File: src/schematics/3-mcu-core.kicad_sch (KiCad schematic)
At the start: 116 parts, among them Q301 NX6008NBKW, U301 PIC32CX1025SG41100-I/E5X, U302 AP22653AW6

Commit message: Added part numbers for the capacitors.
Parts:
- C301, C302, C303, C304, C305, C306, C307, C309, C310, C311, C312, C313, C314, C322, C326, C327, C328, C329, C330, C331, C332, C333, C334, C335, C336, C337, C338, C339, C340, C341, C342, C343, C344, C345, C346, C347, C348, C349, C350: ManufacturerPartNumber (none) -> CL05A475MP5NRNC
- C321: Manufacturer (none) -> Samsung; Manufacturer2 (none) -> Samsung; Manufacturer2PartNumber (none) -> CL05A104KA5NNNC; ManufacturerPartNumber (none) -> CL05B104KA5NNNC
- FB301: Package (none) -> WLBD2012

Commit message: Added part numbers for the resistors.
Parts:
- R301, R302, R303, R304: Manufacturer (none) -> Walsin; Manufacturer2 (none) -> Yageo; Manufacturer2PartNumber (none) -> RC0402FR-0710KL; ManufacturerPartNumber (none) -> WR04X1002FTL
- R305, R306, R320: Manufacturer (none) -> Walsin; Manufacturer2 (none) -> Yageo; Manufacturer2PartNumber (none) -> RC0402FR-071KL; ManufacturerPartNumber (none) -> WR04X1001FTL
- R307, R309: Manufacturer (none) -> Yageo; Manufacturer2 (none) -> Walsin; Manufacturer2PartNumber (none) -> WR04X000PTL; ManufacturerPartNumber (none) -> RC0402FR-070RL
- R310, R332, R333, R348, R349, R350: Manufacturer (none) -> Walsin; Manufacturer2 (none) -> Yageo; Manufacturer2PartNumber (none) -> RC0402FR-0733KL; ManufacturerPartNumber (none) -> WR04X3302FTL
- R311, R312, R313, R314, R315, R316, R317, R321, R322, R323, R324, R325, R326, R327, R328, R329, R330, R331, R336, R337, R338, R339, R340: Manufacturer (none) -> Yageo; Manufacturer2 (none) -> Bourns; Manufacturer2PartNumber (none) -> CR0402-FX-43R0GLF; ManufacturerPartNumber (none) -> RC0402FR-0743RL
- R318, R319, R346, R347: Manufacturer (none) -> Yageo; Manufacturer2 (none) -> Walsin; Manufacturer2PartNumber (none) -> MR04X1801FTL; ManufacturerPartNumber (none) -> RC0402FR-071K8L
- R334, R335: Manufacturer (none) -> Walsin; Manufacturer2 (none) -> Yageo; Manufacturer2PartNumber (none) -> RC0402FR-07330RL; ManufacturerPartNumber (none) -> WR04X3300FTL
- R341, R342, R343, R344, R345: Manufacturer (none) -> Yageo; Manufacturer2 (none) -> KOA Speer; Manufacturer2PartNumber (none) -> RK73H1ETTP41R2F; ManufacturerPartNumber (none) -> RC0402FR-0741R2L
- R351, R352: Manufacturer (none) -> Yageo; Manufacturer2 (none) -> Yageo; Manufacturer2PartNumber (none) -> AC0402DR-0739KL; ManufacturerPartNumber (none) -> RC0402FR-0739KL

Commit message: Started to clean up the ERC flags.
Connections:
- net at XTAL301.2: no longer XTAL301.4
- net at XTAL302.2: no longer XTAL302.4

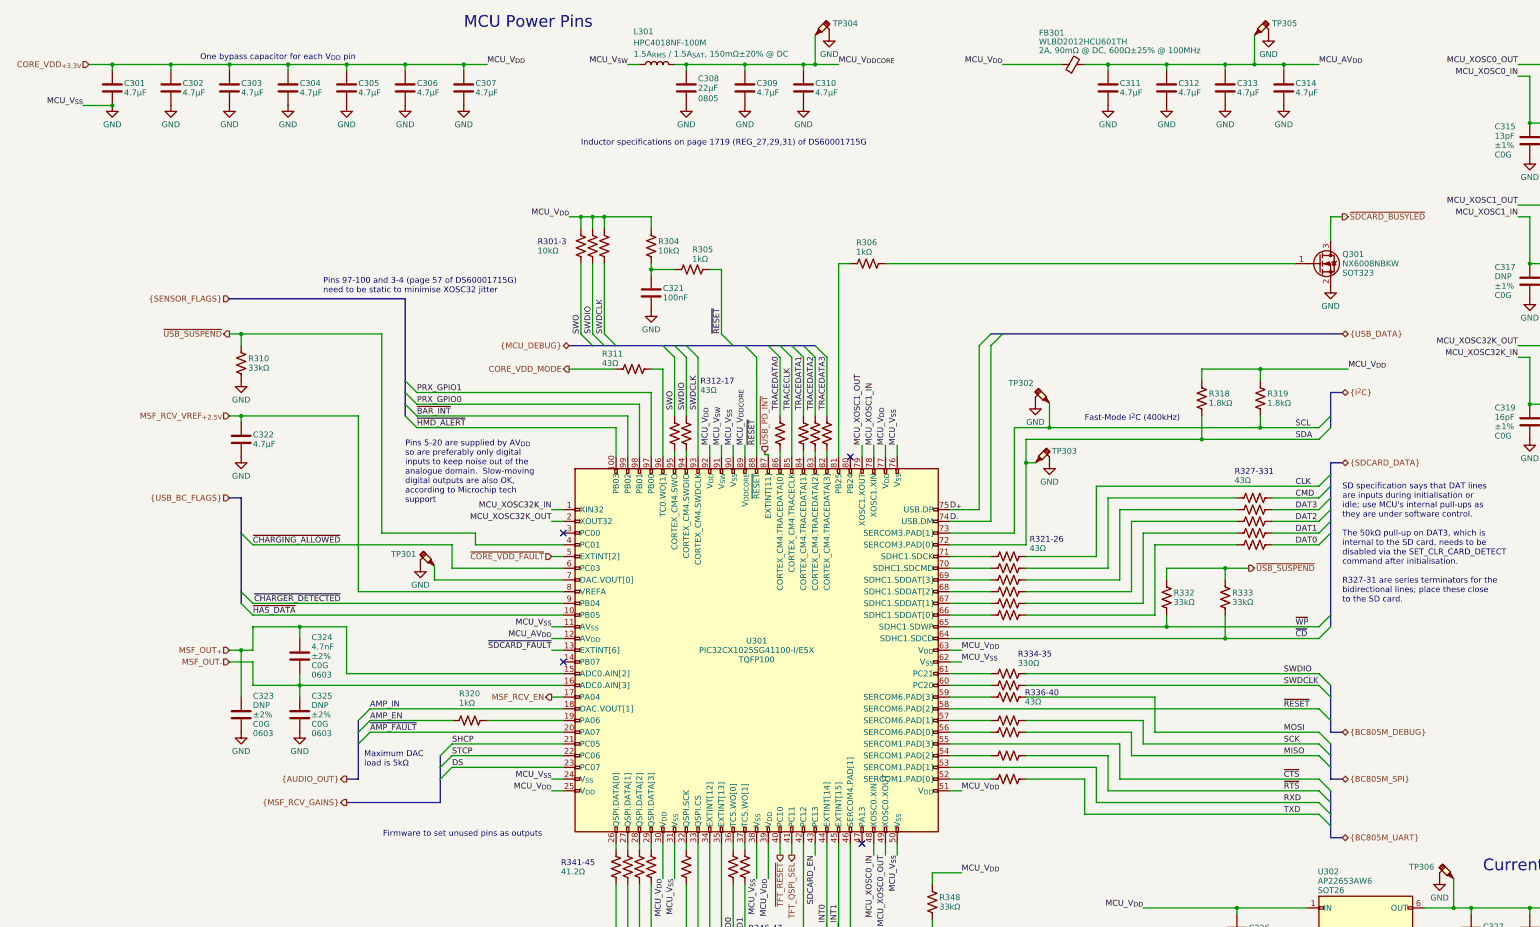
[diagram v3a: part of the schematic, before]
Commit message: Clean up the remaining ERC flags.
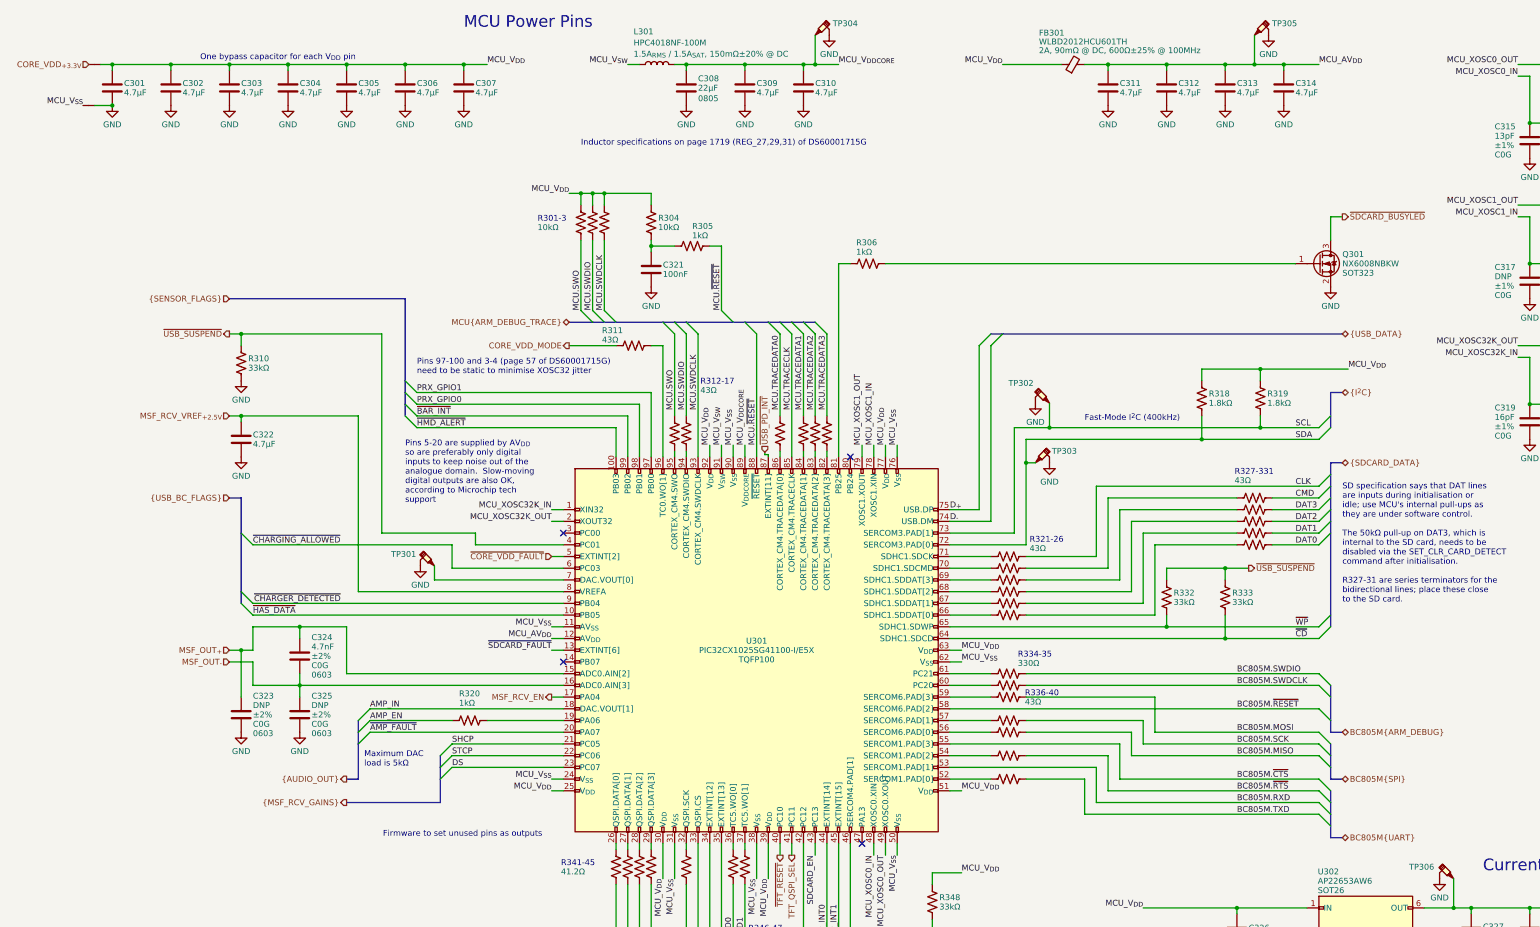
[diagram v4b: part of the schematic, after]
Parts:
- added NT301, NT302: Net Tie, restall-generic-wires:net-tie-2-6mil, symbol restall-generic-wires:net-tie-2
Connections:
- net CORE_VDD_{+3.3V}: now also NT301.1 (P1_PASSIVE); no longer C301.1, C302.1, C303.1, C304.1, C305.1, C306.1, C307.1, C326.1, C337.1, C338.1, C339.1, C340.1, C341.1, C342.1, C343.1, C344.1, C345.1, C346.1, C347.1, C348.1, C349.1, C350.1, FB301.1 (P1), R301.2, R302.2, R303.2, R304.1, R318.1, R319.1, R348.1, U301.25 (V_{DD}), U301.30 (V_{DD}), U301.39 (V_{DD}), U301.51 (V_{DD}), U301.63 (V_{DD}), U301.77 (V_{DD}), U301.92 (V_{DD}), U302.1 (IN)
- net SCK: no longer R337.2
- net GND renamed GND_PWRIN
- net GND_PWRIN: now also NT302.2 (P2_PASSIVE); no longer U301.101 (V_{SS}), U301.11 (AV_{SS}), U301.24 (V_{SS}), U301.31 (V_{SS}), U301.38 (V_{SS}), U301.50 (V_{SS}), U301.62 (V_{SS}), U301.76 (V_{SS}), U301.90 (V_{SS})
- net MISO renamed BC805M.MISO
- net MOSI renamed BC805M.MOSI
- net RXD renamed BC805M.RXD
- net SWDCLK renamed MCU.SWDCLK
- net MCU.SWDCLK: no longer R335.2
- net SWDIO renamed MCU.SWDIO
- net MCU.SWDIO: no longer R334.2
- net SWO renamed MCU.SWO
- net TRACECLK renamed MCU.TRACECLK
- net TRACEDATA0 renamed MCU.TRACEDATA0
- net TRACEDATA1 renamed MCU.TRACEDATA1
- net TRACEDATA2 renamed MCU.TRACEDATA2
- net TRACEDATA3 renamed MCU.TRACEDATA3
- net TXD renamed BC805M.TXD
- net ~{CTS} renamed BC805M.~{CTS}
- net ~{RESET} renamed MCU.~{RESET}
- net MCU.~{RESET}: no longer U301.58 (PC18)
- net ~{RTS} renamed BC805M.~{RTS}
- new net BC805M.SCK: R337.2
- new net BC805M.SWDCLK: R335.2
- new net BC805M.SWDIO: R334.2
- new net BC805M.~{RESET}: U301.58 (PC18)
- new net MCU_V_{DD}: C301.1, C302.1, C303.1, C304.1, C305.1, C306.1, C307.1, C326.1, C337.1, C338.1, C339.1, C340.1, C341.1, C342.1, C343.1, C344.1, C345.1, C346.1, C347.1, C348.1, C349.1, C350.1, FB301.1 (P1), NT301.2 (P2_PASSIVE), R301.2, R302.2, R303.2, R304.1, R318.1, R319.1, R348.1, U301.25 (V_{DD}), U301.30 (V_{DD}), U301.39 (V_{DD}), U301.51 (V_{DD}), U301.63 (V_{DD}), U301.77 (V_{DD}), U301.92 (V_{DD}), U302.1 (IN)
- new net MCU_V_{SS}: NT302.1 (P1_PASSIVE), U301.11 (AV_{SS}), U301.24 (V_{SS}), U301.31 (V_{SS}), U301.38 (V_{SS}), U301.50 (V_{SS}), U301.62 (V_{SS}), U301.76 (V_{SS}), U301.90 (V_{SS})
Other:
- moved on the sheet: C321, R304, R305, R311

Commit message: Started to lay out the PCB.
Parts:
- removed NT301, NT302: Net Tie, restall-generic-wires:net-tie-2-6mil, symbol restall-generic-wires:net-tie-2
- L301: value HPC4018NF-100M -> 10μH
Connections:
- net MCU_V_{DD} is gone; now on net CORE_VDD_{+3.3V}: C301.1, C302.1, C303.1, C304.1, C305.1, C306.1, C307.1, C326.1, C337.1, C338.1, C339.1, C340.1, C341.1, C342.1, C343.1, C344.1, C345.1, C346.1, C347.1, C348.1, C349.1, C350.1, FB301.1 (P1), R301.2, R302.2, R303.2, R304.1, R318.1, R319.1, R348.1, U301.25 (V_{DD}), U301.30 (V_{DD}), U301.39 (V_{DD}), U301.51 (V_{DD}), U301.63 (V_{DD}), U301.77 (V_{DD}), U301.92 (V_{DD}), U302.1 (IN)
- net MCU_V_{SS} is gone; now on net GND: U301.11 (AV_{SS}), U301.24 (V_{SS}), U301.31 (V_{SS}), U301.38 (V_{SS}), U301.50 (V_{SS}), U301.62 (V_{SS}), U301.76 (V_{SS}), U301.90 (V_{SS})
- net D_{+} renamed MCU.D+
- net D_{-} renamed MCU.D-
- net GND_PWRIN renamed GND
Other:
- note added: "TODO: GND_PWRIN IS ACTUALLY GND - HOW TO RENAME THE DAMN NET ?!?"

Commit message: Rearranged the SD Card and TVS placements.
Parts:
- removed R327, R328, R329, R330, R331: 43Ω, restall-generic-resistors:nominal-0402-1005, symbol restall-generic-resistors:resistor
- renumbered R332 to R327, R333 to R328, R334 to R329, R335 to R330, R336 to R331, R337 to R332, R338 to R333, R339 to R334, R340 to R335, R341 to R336, R342 to R337, R343 to R338, R344 to R339, R345 to R340, R346 to R341, R347 to R342, R348 to R343, R349 to R344, R350 to R345, R351 to R346, R352 to R347
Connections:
- net CMD: now also R322.2
- net DAT0: now also R326.2
- net DAT1: now also R325.2
- net DAT2: now also R324.2
- net DAT3: now also R323.2
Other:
- note added: "R329-30"
- note added: "R331-35"
- note added: "R341-42"
- note added: "SD specification says that DAT lines are inputs during initialisation or idle; use MCU's internal pull-ups as they are under software control. The 50kΩ pull-up on DAT3, which is internal to the SD card, needs to be disabled via the SET_CLR_CARD_DETECT command after initialisation."
- note removed: "R327-331"
- note removed: "R334-35"
- note removed: "R341-45"
- note removed: "R346-47"
- note removed: "SD specification says that DAT lines are inputs during initialisation or idle; use MCU's internal pull-ups as they are under software control. The 50kΩ pull-up on DAT3, which is internal to the SD card, needs to be disabled via the SET_CLR_CARD_DETECT command after initialisation. R327-31 are series terminators for the bidirectional lines; place these close to the SD card."

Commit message: PCB routing.
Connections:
- net DS: now also U301.21 (PC05); no longer U301.23 (PC07)
- net SHCP: now also U301.23 (PC07); no longer U301.21 (PC05)
- net MSF_OUT_{+} renamed MSF_OUT+
- net MSF_OUT_{-} renamed MSF_OUT-
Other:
- note removed: "TODO: GND_PWRIN IS ACTUALLY GND - HOW TO RENAME THE DAMN NET ?!?"
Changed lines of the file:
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@@
-    (effects (font (size 1.27 1.27)) (justify left bottom))
-  )
-  (text "TODO: GND_PWRIN IS ACTUALLY GND - HOW TO RENAME THE DAMN NET ?!?"
-    (at 21.082 53.594 0)
     (effects (font (size 1.27 1.27)) (justify left bottom))
   )
@@
     (effects (font (size 1.27 1.27)) (justify left bottom))
   )
-  (label "DS" (at 111.76 177.8 0) (fields_autoplaced)
+  (label "DS" (at 111.76 172.72 0) (fields_autoplaced)
     (effects (font (size 1.27 1.27)) (justify left bottom))
   )
@@
     (effects (font (size 1.27 1.27)) (justify left bottom))
   )
-  (label "SHCP" (at 111.76 172.72 0) (fields_autoplaced)
+  (label "SHCP" (at 111.76 177.8 0) (fields_autoplaced)
     (effects (font (size 1.27 1.27)) (justify left bottom))
   )
@@
     (effects (font (size 1.27 1.27)) (justify right))
   )
-  (hierarchical_label "MSF_OUT_{+}" (shape input) (at 63.5 152.4 180) (fields_autoplaced)
+  (hierarchical_label "MSF_OUT+" (shape input) (at 63.5 152.4 180) (fields_autoplaced)
     (effects (font (size 1.27 1.27)) (justify right))
   )
@@
     (effects (font (size 1.27 1.27)) (justify left))
   )
-  (hierarchical_label "MSF_OUT_{-}" (shape input) (at 63.5 154.94 180) (fields_autoplaced)
-    (effects (font (size 1.27 1.27)) (justify right))
-  )
+  (hierarchical_label "MSF_OUT-" (shape input) (at 63.5 154.94 180) (fields_autoplaced)
+    (effects (font (size 1.27 1.27)) (justify right))
+  )

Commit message: PCB routing.
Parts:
- removed R320: 1kΩ, restall-generic-resistors:nominal-0402-1005, symbol restall-generic-resistors:resistor
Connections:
- net AMP_EN: now also U301.19 (PA06)
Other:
- note added: "TODO: R320 HAS BEEN REMOVED - RENAME R321 -> R320, ETC."
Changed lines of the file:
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@@
     (stroke (width 0) (type default))
   )
-  (wire (pts (xy 93.98 167.64) (xy 111.76 167.64))
-    (stroke (width 0) (type default))
-  )
   (wire (pts (xy 279.4 149.86) (xy 299.72 149.86))
     (stroke (width 0) (type default))
@@
     (stroke (width 0) (type default))
   )
-  (wire (pts (xy 119.38 167.64) (xy 135.89 167.64))
+  (wire (pts (xy 93.98 167.64) (xy 135.89 167.64))
     (stroke (width 0) (type default))
   )
@@
     (effects (font (size 1.27 1.27)) (justify left bottom))
   )
+  (text "TODO: R320 HAS BEEN REMOVED - RENAME R321 -> R320, ETC."
+    (at -7.874 171.704 0)
+    (effects (font (size 1.27 1.27)) (justify left bottom))
+  )
   (text "R331-35" (at 235.966 162.56 0)
     (effects (font (size 1.27 1.27)) (justify left bottom))
@@
         )
       )
-    )
-  )
-  (symbol (lib_id "restall-generic-resistors:resistor") (at 115.57 167.64 90) (unit 1)
-    (in_bom yes) (on_board yes) (dnp no)
-    (property "Reference" "R320" (at 113.284 161.798 90)
-      (effects (font (size 1.27 1.27)) (justify right))
-    )
-    (property "Value" "1kΩ" (at 113.284 163.83 90)
-      (effects (font (size 1.27 1.27)) (justify right))
-    )
-    (property "Footprint" "restall-generic-resistors:nominal-0402-1005" (at 115.824 166.624 90)
-      (effects (font (size 1.27 1.27)) (justify left) hide)
-    )
-    (property "Datasheet" "~" (at 115.57 167.64 0)
-      (effects (font (size 1.27 1.27)) (justify left) hide)
-    )
-    (property "Label" "1kΩ±1% 0.0625W" (at 117.094 165.862 0)
-      (effects (font (size 1.27 1.27)) (justify left) hide)
-    )
-    (property "Tolerance" "±1%" (at 119.126 165.862 0)
-      (effects (font (size 1.27 1.27)) (justify left) hide)
-    )
-    (property "PowerRating" "0.0625W" (at 121.158 165.862 0)
-      (effects (font (size 1.27 1.27)) (justify left) hide)
-    )
-    (property "TemperatureCoefficient" "±100ppm" (at 123.19 165.862 0)
-      (effects (font (size 1.27 1.27)) (justify left) hide)
-    )
-    (property "Construction" "Thick Film" (at 125.222 165.862 0)
-      (effects (font (size 1.27 1.27)) (justify left) hide)
-    )
-    (property "Package" "0402" (at 127.254 165.862 0)
-      (effects (font (size 1.27 1.27)) (justify left) hide)
-    )
-    (property "Manufacturer" "Walsin" (at 115.57 167.64 0)
-      (effects (font (size 1.27 1.27)) (justify left) hide)
-    )
-    (property "ManufacturerPartNumber" "WR04X1001FTL" (at 115.57 167.64 0)
-      (effects (font (size 1.27 1.27)) (justify left) hide)
-    )
-    (property "Manufacturer2" "Yageo" (at 115.57 167.64 0)
-      (effects (font (size 1.27 1.27)) (justify left) hide)
-    )
-    (property "Manufacturer2PartNumber" "RC0402FR-071KL" (at 115.57 167.64 0)
-      (effects (font (size 1.27 1.27)) (justify left) hide)
-    )
-    (pin "1")
-    (pin "2")
-    (instances
-      (project "msf-owl-clock"
-        (path "/56d623d3-22db-4d43-a9d9-e6bb4bb68946/cc278a5b-e802-444a-81ef-f38d11985404"
-          (reference "R320") (unit 1)
-        )
-      )
